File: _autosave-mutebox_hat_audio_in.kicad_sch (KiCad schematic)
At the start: 39 parts, among them J1 GPIO, J3 RCJ-042, J4 RCJ-042, U2 74LVC157, U3 PCM1862DBT, Y3 XO32

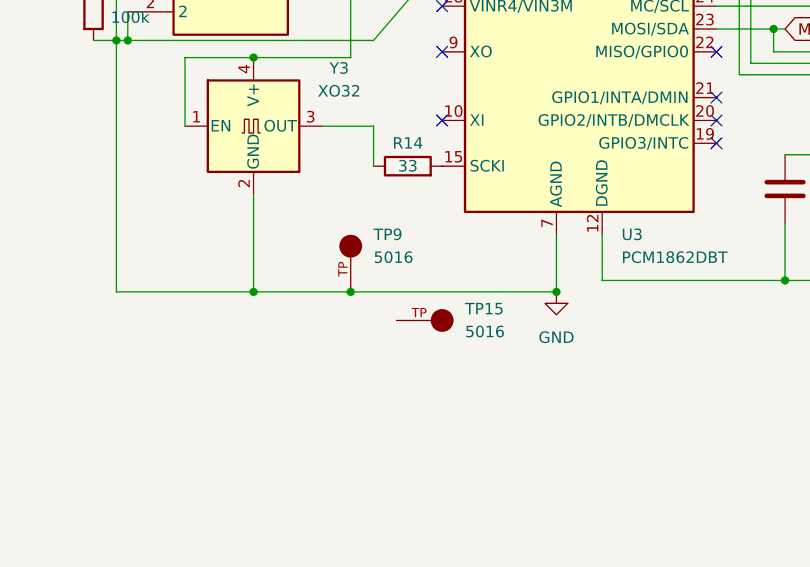
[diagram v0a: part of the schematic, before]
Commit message: Added testpoint with large clip on footprint
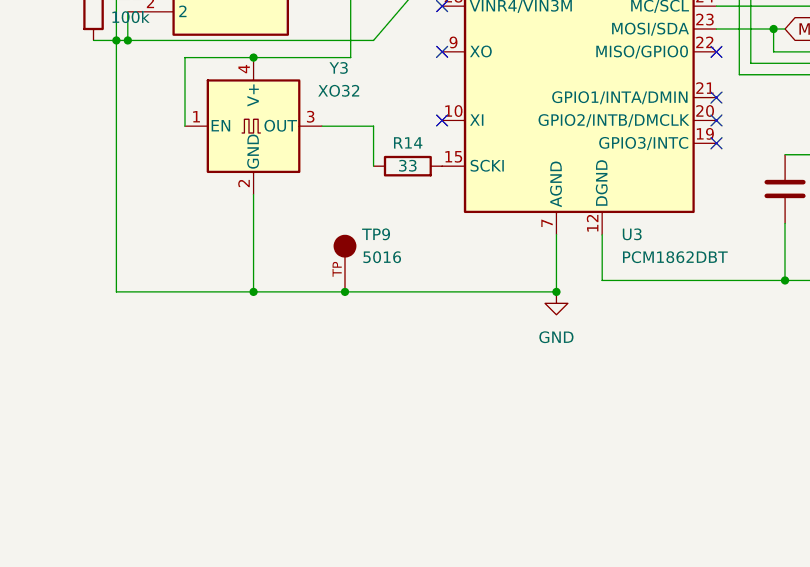
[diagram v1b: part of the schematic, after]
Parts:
- removed TP15: 5016, 5016:KEYSTONE_5016, symbol TestPoint:5016
- TP9: footprint 5016:KEYSTONE_5016 -> Connector:KEYSTONE_5016

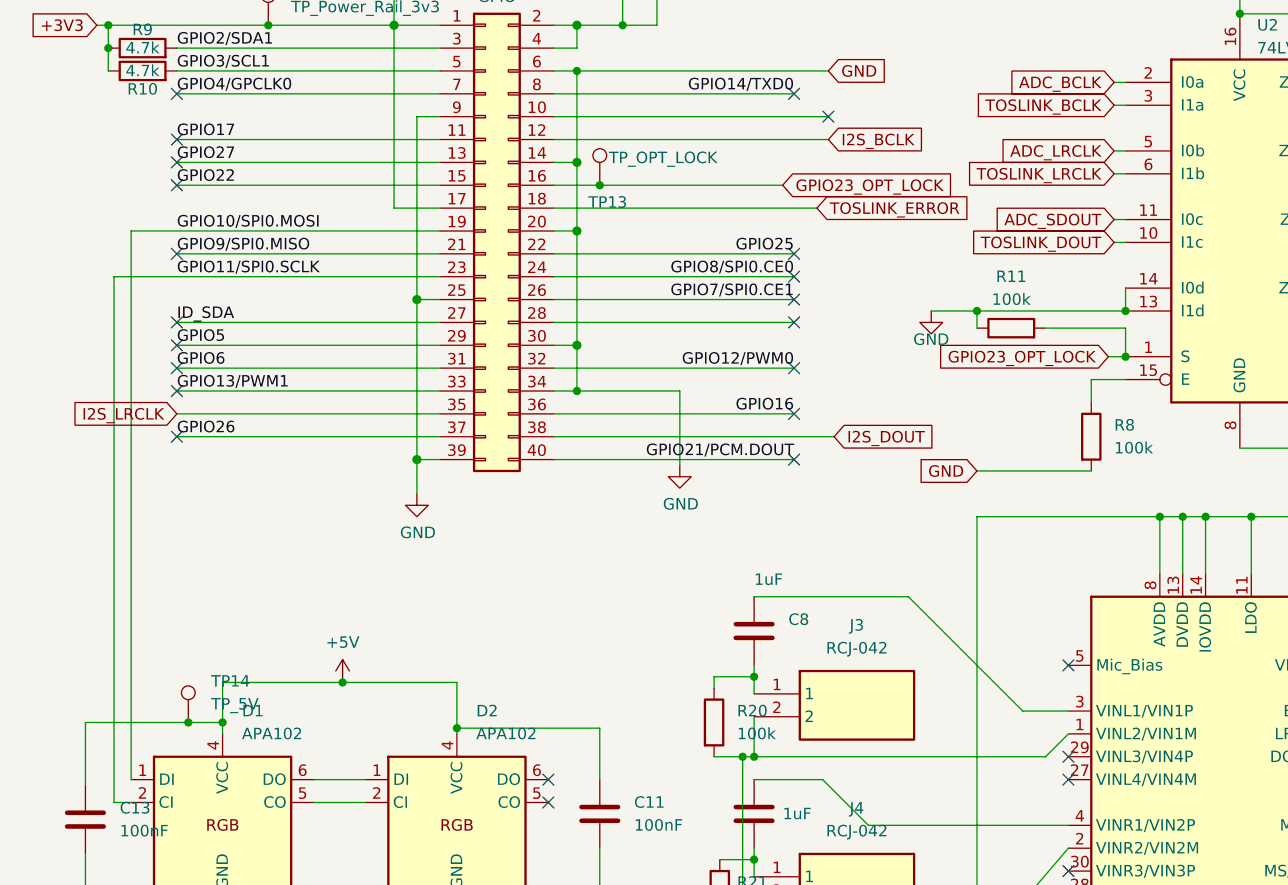
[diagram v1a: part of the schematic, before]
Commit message: Fixed dotstar positioning.  Minor changes to PCB
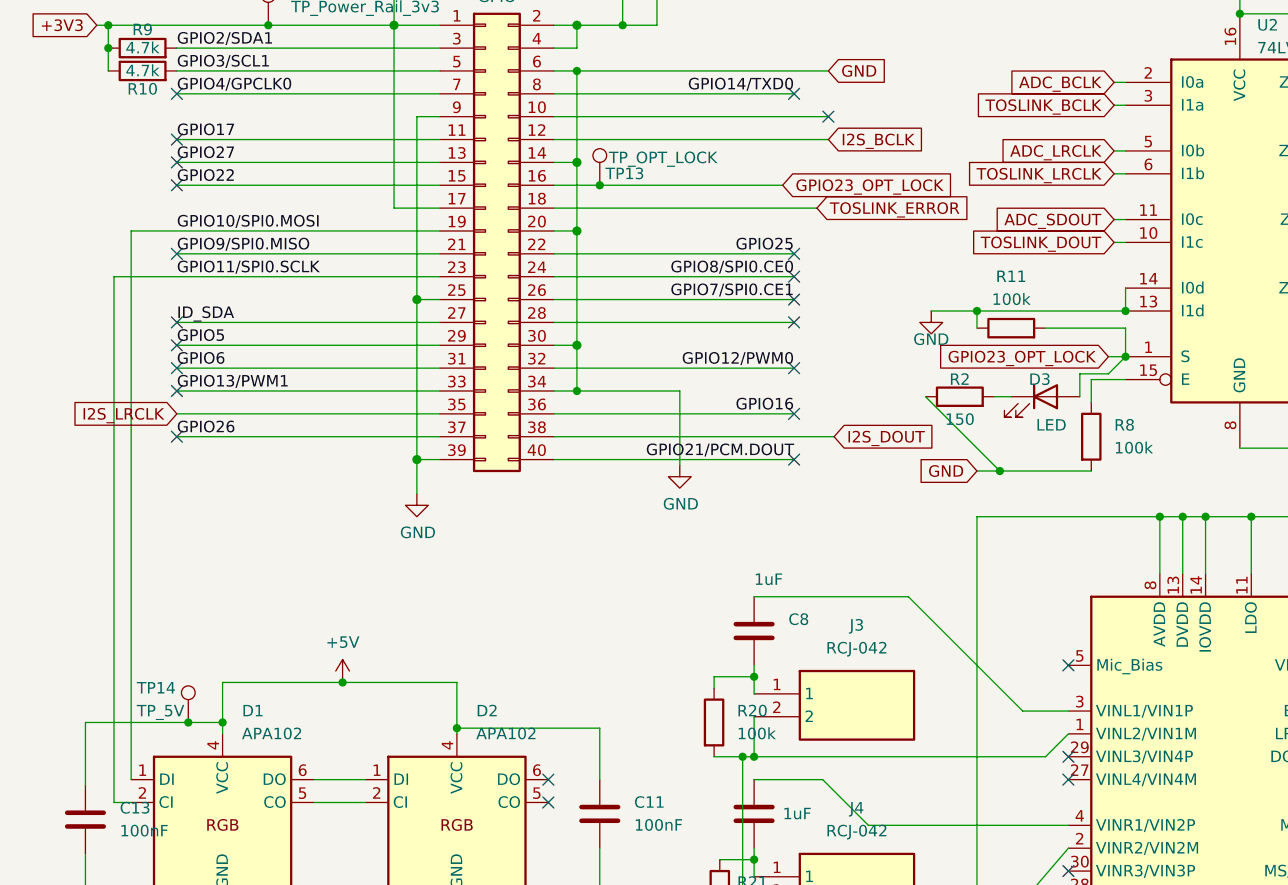
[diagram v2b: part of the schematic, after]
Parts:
- added D3: LED, LED_SMD:LED_0805_2012Metric_Pad1.15x1.40mm_HandSolder, symbol Device:LED
- added R2: 150, Resistor_SMD:R_0805_2012Metric_Pad1.20x1.40mm_HandSolder, symbol Device:R
- TP9: footprint Connector:KEYSTONE_5016 -> 5016:KEYSTONE_5016
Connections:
- net GND: now also R2.1
- net GPIO23_OPT_LOCK: now also D3.2 (A)
- new net: D3.1 (K), R2.2
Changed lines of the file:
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@@
 	)
 	(junction
+		(at 123.19 77.47)
+		(diameter 0)
+		(color 0 0 0 0)
+	)
+	(junction
 		(at 167.64 127)
 		(diameter 0)
@@
 	(wire
 		(pts
+			(xy 132.08 66.675) (xy 135.255 66.675)
+		)
+		(stroke
+			(width 0)
+			(type default)
+		)
+	)
+	(wire
+		(pts
 			(xy 173.99 82.55) (xy 180.34 82.55)
 		)
@@
 	(wire
 		(pts
+			(xy 135.255 66.675) (xy 137.16 64.77)
+		)
+		(stroke
+			(width 0)
+			(type default)
+		)
+	)
+	(wire
+		(pts
 			(xy 92.075 120.65) (xy 95.885 120.65)
 		)
@@
 	(wire
 		(pts
+			(xy 122.555 69.215) (xy 124.46 69.215)
+		)
+		(stroke
+			(width 0)
+			(type default)
+		)
+	)
+	(wire
+		(pts
 			(xy 62.865 127) (xy 62.865 131.445)
 		)
@@
 	(wire
 		(pts
+			(xy 114.935 69.215) (xy 123.19 77.47)
+		)
+		(stroke
+			(width 0)
+			(type default)
+		)
+	)
+	(wire
+		(pts
 			(xy 73.66 48.26) (xy 102.87 48.26)
 		)
@@
 	(wire
 		(pts
+			(xy 132.08 66.675) (xy 132.08 69.215)
+		)
+		(stroke
+			(width 0)
+			(type default)
+		)
+	)
+	(wire
+		(pts
 			(xy 193.04 154.94) (xy 187.96 154.94)
 		)
@@
 	(wire
 		(pts
+			(xy 123.19 77.47) (xy 133.35 77.47)
+		)
+		(stroke
+			(width 0)
+			(type default)
+		)
+	)
+	(wire
+		(pts
 			(xy 36.83 131.445) (xy 50.8 131.445)
 		)
@@
 	(wire
 		(pts
-			(xy 120.65 77.47) (xy 133.35 77.47)
+			(xy 120.65 77.47) (xy 123.19 77.47)
 		)
 		(stroke
@@
 	)
 	(symbol
+		(lib_id "Device:LED")
+		(at 128.27 69.215 0)
+		(unit 1)
+		(exclude_from_sim no)
+		(in_bom yes)
+		(on_board yes)
+		(dnp no)
+		(property "Reference" "D3"
+			(at 127.635 67.31 0)
+			(effects
+				(font
+					(size 1.27 1.27)
+				)
+			)
+		)
+		(property "Value" "LED"
+			(at 128.905 72.39 0)
+			(effects
+				(font
+					(size 1.27 1.27)
+				)
+			)
+		)
+		(property "Footprint" "LED_SMD:LED_0805_2012Metric_Pad1.15x1.40mm_HandSolder"
+			(at 128.27 69.215 0)
+			(effects
+				(font
+					(size 1.27 1.27)
+				)
+				(hide yes)
+			)
+		)
+		(property "Datasheet" "~"
+			(at 128.27 69.215 0)
+			(effects
+				(font
+					(size 1.27 1.27)
+				)
+				(hide yes)
+			)
+		)
+		(property "Description" "Light emitting diode"
+			(at 128.27 69.215 0)
+			(effects
+				(font
+					(size 1.27 1.27)
+				)
+				(hide yes)
+			)
+		)
+		(property "Sim.Pins" "1=K 2=A"
+			(at 128.27 69.215 0)
+			(effects
+				(font
+					(size 1.27 1.27)
+				)
+				(hide yes)
+			)
+		)
+		(pin "1"
+		)
+		(pin "2"
+		)
+		(instances
+			(project "mutebox_hat_audio_in"
+				(path "/e63e39d7-6ac0-4ffd-8aa3-1841a4541b55"
+					(reference "D3")
+					(unit 1)
+				)
+			)
+		)
+	)
+	(symbol
 		(lib_id "Device:R")
 		(at 91.44 105.41 0)
@@
 			)
 		)
-		(property "Footprint" "Connector:KEYSTONE_5016"
+		(property "Footprint" "5016:KEYSTONE_5016"
 			(at 120.015 151.13 0)
 			(effects
@@
 	)
 	(symbol
+		(lib_id "Device:R")
+		(at 118.745 69.215 90)
+		(unit 1)
+		(exclude_from_sim no)
+		(in_bom yes)
+		(on_board yes)
+		(dnp no)
+		(property "Reference" "R2"
+			(at 118.745 67.31 90)
+			(effects
+				(font
+					(size 1.27 1.27)
+				)
+			)
+		)
+		(property "Value" "150"
+			(at 118.745 71.755 90)
+			(effects
+				(font
+					(size 1.27 1.27)
+				)
+			)
+		)
+		(property "Footprint" "Resistor_SMD:R_0805_2012Metric_Pad1.20x1.40mm_HandSolder"
+			(at 118.745 70.993 90)
+			(effects
+				(font
+					(size 1.27 1.27)
+				)
+				(hide yes)
+			)
+		)
+		(property "Datasheet" "~"
+			(at 118.745 69.215 0)
+			(effects
+				(font
+					(size 1.27 1.27)
+				)
+				(hide yes)
+			)
+		)
+		(property "Description" "Resistor"
+			(at 118.745 69.215 0)
+			(effects
+				(font
+					(size 1.27 1.27)
+				)
+				(hide yes)
+			)
+		)
+		(pin "2"
+		)
+		(pin "1"
+		)
+		(instances
+			(project "mutebox_hat_audio_in"
+				(path "/e63e39d7-6ac0-4ffd-8aa3-1841a4541b55"
+					(reference "R2")
+					(unit 1)
+				)
+			)
+		)
+	)
+	(symbol
 		(lib_id "power:GND")
 		(at 143.51 156.21 0)
@@
 		(on_board yes)
 		(dnp no)
-		(fields_autoplaced yes)
 		(property "Reference" "TP14"
-			(at 35.56 100.8379 0)
+			(at 27.305 101.6 0)
 			(effects
 				(font
@@
 		)
 		(property "Value" "TP_5V"
-			(at 35.56 103.3779 0)
+			(at 27.305 104.14 0)
 			(effects
 				(font
@@
 		(dnp no)
 		(property "Reference" "TP13"
-			(at 77.47 47.625 0)
+			(at 79.375 44.45 0)
 			(effects
 				(font
